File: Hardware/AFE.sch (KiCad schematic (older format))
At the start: 39 parts, among them U801 4069.HEF4069UBTT,118, U802 MCP47CXBX2

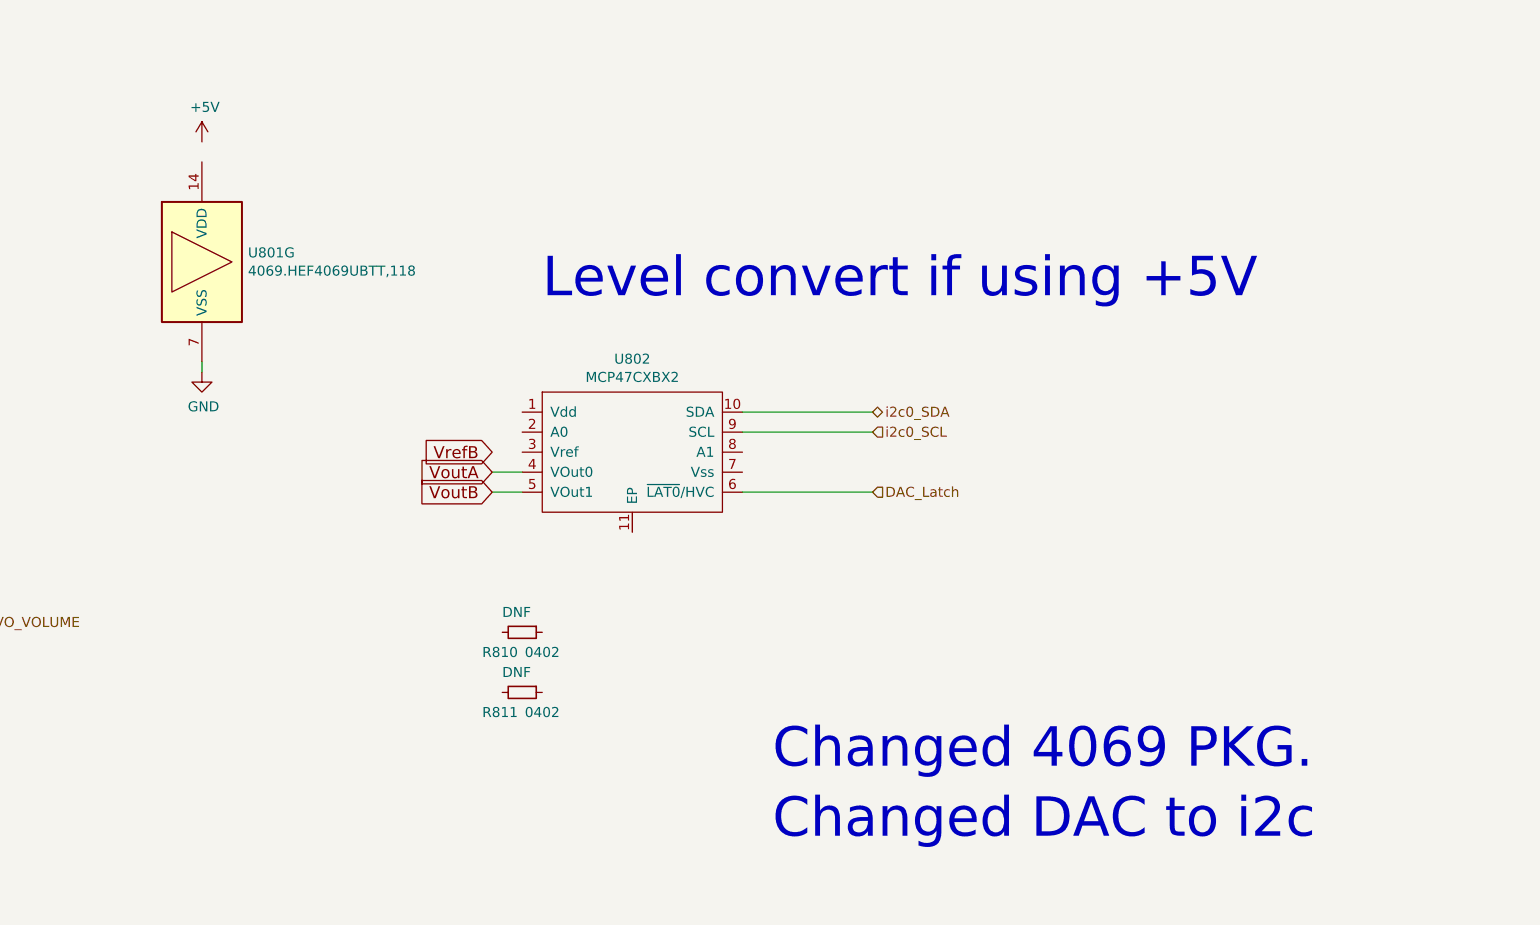
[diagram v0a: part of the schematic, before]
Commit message: Level shifting for DAC, some connectivity.
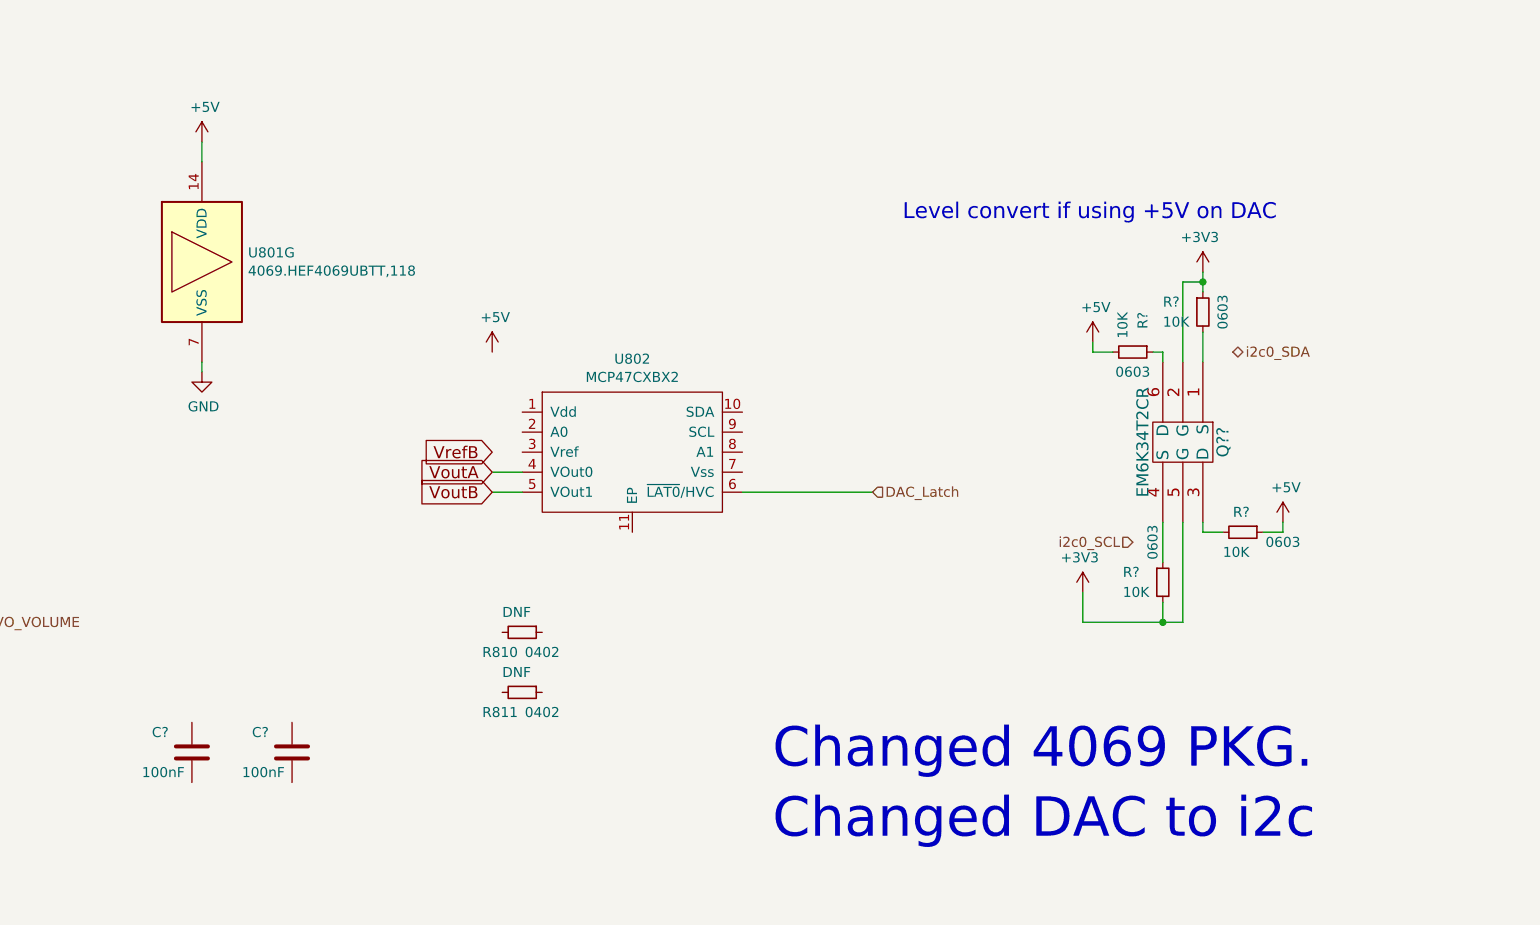
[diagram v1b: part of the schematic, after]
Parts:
- added C? (x2): 100nF, Capacitor_SMD:C_0603_1608Metric_Pad1.08x0.95mm_HandSolder, symbol Device:C
- added Q??: EM6K34T2CR, OHMC2022:DualNFet.SOT563.EM6K34T2CR, symbol OHMC2022:EM6K34T2CR
- added R? (x4): 10K, Resistor_SMD:R_0603_1608Metric, symbol Device:R_Small
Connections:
- net +5V: now also U801.14 (VDD), R?.1, R?.2
- net i2c0_SCL: no longer U802.9 (SCL)
- net i2c0_SDA: no longer U802.10 (SDA)
- new net: Q??.1 (S), R?.2
- new net: Q??.3 (D), R?.2
- new net: Q??.4 (S), R?.1
- new net: Q??.6 (D), R?.1
- new net +3V3: Q??.2 (G), Q??.5 (G), R?.1, R?.2
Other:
- note added: "Level convert if using +5V on DAC"
- note removed: "Level convert if using +5V"
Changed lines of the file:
@@
 Text GLabel 6750 4600 0    60   Input ~ 0
 VoutB
-Text Notes 7000 3650 0    197  ~ 0
-Level convert if using +5V
+Text Notes 8800 3250 0    79   ~ 0
+Level convert if using +5V on DAC
 $Comp
 L Connector:TestPoint TP801
@@
 Text HLabel 4200 5250 2    50   Output ~ 0
 VO_VOLUME
-Text HLabel 8650 4200 2    50   BiDi ~ 0
+Text HLabel 10450 3900 2    50   BiDi ~ 0
 i2c0_SDA
-Text HLabel 8650 4300 2    50   Input ~ 0
+Text HLabel 9950 4850 0    50   Input ~ 0
 i2c0_SCL
 Text HLabel 8650 4600 2    50   Input ~ 0
@@
 Wire Wire Line
 	8000 4600 8650 4600
-Wire Wire Line
-	8650 4300 8000 4300
-Wire Wire Line
-	8000 4200 8650 4200
 $Comp
 L OHMC2022:4069.HEF4069UBTT,118 U801
@@
 Wire Wire Line
 	1050 6900 1050 7000
+$Comp
+L OHMC2022:EM6K34T2CR Q??
+U 1 1 613FBC97
+P 10200 4350
+F 0 "Q??" H 10200 4550 60  0000 C CNN
+F 1 "EM6K34T2CR" H 10200 4150 60  0000 C CNN
+F 2 "OHMC2022:DualNFet.SOT563.EM6K34T2CR" H 11200 4590 60  0001 C CNN
+F 3 "https://fscdn.rohm.com/en/products/databook/datasheet/discrete/transistor/mosfet/em6k34.pdf" H 10200 4601 60  0001 C CNN
+F 4 "EM6K34T2CR" H 10950 4700 50  0001 C CNN "MPN"
+F 5 "EM6K34T2CRCT-ND" H 11700 4700 50  0001 C CNN "DPN"
+	1    10200 4350
+	0    1    1    0
+$EndComp
+$Comp
+L Device:C C?
+U 1 1 6140B8D2
+P 5750 5900
+F 0 "C?" H 5550 6000 50  0000 L CNN
+F 1 "100nF" H 5500 5800 50  0000 L CNN
+F 2 "Capacitor_SMD:C_0603_1608Metric_Pad1.08x0.95mm_HandSolder" H 5788 5750 50  0001 C CNN
+F 3 "" H 5750 5900 50  0000 C CNN
+	1    5750 5900
+	1    0    0    -1
+$EndComp
+$Comp
+L Device:C C?
+U 1 1 6140CB4F
+P 5250 5900
+F 0 "C?" H 5050 6000 50  0000 L CNN
+F 1 "100nF" H 5000 5800 50  0000 L CNN
+F 2 "Capacitor_SMD:C_0603_1608Metric_Pad1.08x0.95mm_HandSolder" H 5288 5750 50  0001 C CNN
+F 3 "" H 5250 5900 50  0000 C CNN
+	1    5250 5900
+	1    0    0    -1
+$EndComp
+$Comp
+L Device:R_Small R?
+U 1 1 614210B0
+P 10300 3700
+AR Path="/611E335F/614210B0" Ref="R?"  Part="1"
+AR Path="/614210B0" Ref="R?"  Part="1"
+AR Path="/612429E8/614210B0" Ref="R?"  Part="1"
+F 0 "R?" H 10100 3750 50  0000 L CNN
+F 1 "10K" H 10100 3650 50  0000 L CNN
+F 2 "Resistor_SMD:R_0603_1608Metric" V 10230 3700 50  0001 C CNN
+F 3 "~" H 10300 3700 50  0001 C CNN
+F 4 "0603" V 10400 3700 50  0000 C CNN "Pkg"
+F 5 "RNCP0603FTD10K0" H 10300 3700 50  0001 C CNN "MPN"
+F 6 "RNCP0603FTD10K0CT-ND" H 10300 3700 50  0001 C CNN "DPN"
+	1    10300 3700
+	1    0    0    -1
+$EndComp
+$Comp
+L Device:R_Small R?
+U 1 1 614261D7
+P 9950 3900
+AR Path="/611E335F/614261D7" Ref="R?"  Part="1"
+AR Path="/614261D7" Ref="R?"  Part="1"
+AR Path="/612429E8/614261D7" Ref="R?"  Part="1"
+F 0 "R?" H 9750 3950 50  0000 L CNN
+F 1 "10K" H 9750 3850 50  0000 L CNN
+F 2 "Resistor_SMD:R_0603_1608Metric" V 9880 3900 50  0001 C CNN
+F 3 "~" H 9950 3900 50  0001 C CNN
+F 4 "0603" V 10050 3900 50  0000 C CNN "Pkg"
+F 5 "RNCP0603FTD10K0" H 9950 3900 50  0001 C CNN "MPN"
+F 6 "RNCP0603FTD10K0CT-ND" H 9950 3900 50  0001 C CNN "DPN"
+	1    9950 3900
+	0    1    1    0
+$EndComp
+$Comp
+L Device:R_Small R?
+U 1 1 61426AF8
+P 10500 4800
+AR Path="/611E335F/61426AF8" Ref="R?"  Part="1"
+AR Path="/61426AF8" Ref="R?"  Part="1"
+AR Path="/612429E8/61426AF8" Ref="R?"  Part="1"
+F 0 "R?" V 10400 4750 50  0000 L CNN
+F 1 "10K" V 10600 4700 50  0000 L CNN
+F 2 "Resistor_SMD:R_0603_1608Metric" V 10430 4800 50  0001 C CNN
+F 3 "~" H 10500 4800 50  0001 C CNN
+F 4 "0603" V 10550 5000 50  0000 C CNN "Pkg"
+F 5 "RNCP0603FTD10K0" H 10500 4800 50  0001 C CNN "MPN"
+F 6 "RNCP0603FTD10K0CT-ND" H 10500 4800 50  0001 C CNN "DPN"
+	1    10500 4800
+	0    1    1    0
+$EndComp
+$Comp
+L Device:R_Small R?
+U 1 1 61427521
+P 10100 5050
+AR Path="/611E335F/61427521" Ref="R?"  Part="1"
+AR Path="/61427521" Ref="R?"  Part="1"
+AR Path="/612429E8/61427521" Ref="R?"  Part="1"
+F 0 "R?" H 9900 5100 50  0000 L CNN
+F 1 "10K" H 9900 5000 50  0000 L CNN
+F 2 "Resistor_SMD:R_0603_1608Metric" V 10030 5050 50  0001 C CNN
+F 3 "~" H 10100 5050 50  0001 C CNN
+F 4 "0603" V 10050 5250 50  0000 C CNN "Pkg"
+F 5 "RNCP0603FTD10K0" H 10100 5050 50  0001 C CNN "MPN"
+F 6 "RNCP0603FTD10K0CT-ND" H 10100 5050 50  0001 C CNN "DPN"
+	1    10100 5050
+	1    0    0    -1
+$EndComp
+$Comp
+L power:+5V #PWR?
+U 1 1 6142CCFA
+P 6750 3900
+AR Path="/6123BB15/6142CCFA" Ref="#PWR?"  Part="1"
+AR Path="/611E335F/6142CCFA" Ref="#PWR?"  Part="1"
+AR Path="/612429E8/6142CCFA" Ref="#PWR?"  Part="1"
+F 0 "#PWR?" H 6750 3750 50  0001 C CNN
+F 1 "+5V" H 6765 4073 50  0000 C CNN
+F 2 "" H 6750 3900 50  0001 C CNN
+F 3 "" H 6750 3900 50  0001 C CNN
+	1    6750 3900
+	1    0    0    -1
+$EndComp
+Wire Wire Line
+	5300 2850 5300 2950
+$Comp
+L power:+5V #PWR?
+U 1 1 6143609C
+P 10700 4750
+AR Path="/6123BB15/6143609C" Ref="#PWR?"  Part="1"
+AR Path="/611E335F/6143609C" Ref="#PWR?"  Part="1"
+AR Path="/612429E8/6143609C" Ref="#PWR?"  Part="1"
+F 0 "#PWR?" H 10700 4600 50  0001 C CNN
+F 1 "+5V" H 10715 4923 50  0000 C CNN
+F 2 "" H 10700 4750 50  0001 C CNN
+F 3 "" H 10700 4750 50  0001 C CNN
+	1    10700 4750
+	1    0    0    -1
+$EndComp
+$Comp
+L power:+5V #PWR?
+U 1 1 61436B56
+P 9750 3850
+AR Path="/6123BB15/61436B56" Ref="#PWR?"  Part="1"
+AR Path="/611E335F/61436B56" Ref="#PWR?"  Part="1"
+AR Path="/612429E8/61436B56" Ref="#PWR?"  Part="1"
+F 0 "#PWR?" H 9750 3700 50  0001 C CNN
+F 1 "+5V" H 9765 4023 50  0000 C CNN
+F 2 "" H 9750 3850 50  0001 C CNN
+F 3 "" H 9750 3850 50  0001 C CNN
+	1    9750 3850
+	1    0    0    -1
+$EndComp
+Wire Wire Line
+	10050 3900 10100 3900
+Wire Wire Line
+	10100 3900 10100 3950
+Wire Wire Line
+	10400 4800 10300 4800
+Wire Wire Line
+	10300 4800 10300 4750
+Wire Wire Line
+	10700 4750 10700 4800
+Wire Wire Line
+	10700 4800 10600 4800
+Wire Wire Line
+	9750 3850 9750 3900
+Wire Wire Line
+	9750 3900 9850 3900
+$Comp
+L power:+3V3 #PWR?
+U 1 1 614785EE
+P 9700 5100
+AR Path="/611E3335/614785EE" Ref="#PWR?"  Part="1"
+AR Path="/614785EE" Ref="#PWR?"  Part="1"
+F 0 "#PWR?" H 9700 4950 50  0001 C CNN
+F 1 "+3V3" H 9715 5273 50  0000 C CNN
+F 2 "" H 9700 5100 50  0001 C CNN
+F 3 "" H 9700 5100 50  0001 C CNN
+	1    9700 5100
+	-1   0    0    -1
+$EndComp
+$Comp
+L power:+3V3 #PWR?
+U 1 1 6147DD9F
+P 10300 3500
+AR Path="/611E3335/6147DD9F" Ref="#PWR?"  Part="1"
+AR Path="/6147DD9F" Ref="#PWR?"  Part="1"
+F 0 "#PWR?" H 10300 3350 50  0001 C CNN
+F 1 "+3V3" H 10315 3673 50  0000 C CNN
+F 2 "" H 10300 3500 50  0001 C CNN
+F 3 "" H 10300 3500 50  0001 C CNN
+	1    10300 3500
+	-1   0    0    -1
+$EndComp
+Wire Wire Line
+	10300 3500 10300 3550
+Wire Wire Line
+	9700 5100 9700 5250
+Wire Wire Line
+	9700 5250 10100 5250
+Wire Wire Line
+	10100 5250 10100 5150
+Wire Wire Line
+	10100 4950 10100 4750
+Wire Wire Line
+	10200 4750 10200 5250
+Wire Wire Line
+	10200 5250 10100 5250
+Connection ~ 10100 5250
+Wire Wire Line
+	10200 3950 10200 3550
+Wire Wire Line
+	10200 3550 10300 3550
+Connection ~ 10300 3550
+Wire Wire Line
+	10300 3550 10300 3600
+Wire Wire Line
+	10300 3800 10300 3950
 $EndSCHEMATC
